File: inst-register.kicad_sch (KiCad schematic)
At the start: 20 parts

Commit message: Fix Clock
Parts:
- C13: value (none) -> 0.1µF; footprint (none) -> Capacitor_THT:C_Disc_D4.3mm_W1.9mm_P5.00mm
- D26, D27, D28, D29: value (none) -> BLUE; footprint (none) -> LED_THT:LED_D5.0mm
- D30, D31, D32, D33: value (none) -> YELLOW; footprint (none) -> LED_THT:LED_D5.0mm
- R40, R41, R42, R43, R44, R45, R46, R47: value (none) -> 220; footprint (none) -> Resistor_THT:R_Axial_DIN0207_L6.3mm_D2.5mm_P7.62mm_Horizontal
- U13: value (none) -> 74LS245; footprint (none) -> Package_DIP:DIP-20_W7.62mm
- U14, U15: value (none) -> 74LS173; footprint (none) -> Package_DIP:DIP-16_W7.62mm

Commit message: Fix
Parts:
- D26, D27, D28, D29, D30, D31, D32, D33: symbol Device:LED_ALT -> Device:LED
- U13: symbol 8bit-computer-rescue:74LS245 -> 74xx:74LS245
- U14, U15: symbol 8bit-computer-rescue:74LS173 -> 74xx:74LS173
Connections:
- net IR_4: now also D29.2 (A)
- net IR_5: now also D28.2 (A)
- net IR_6: now also D27.2 (A)
- net IR_7: now also D26.2 (A)
- net at R44.1: now also D30.1 (K)
- net at R40.1: now also D26.1 (K)
- net at R41.1: now also D27.1 (K)
- net at R42.1: now also D28.1 (K)
- net at R43.1: now also D29.1 (K)
- net at R45.1: now also D31.1 (K)
- net at R46.1: now also D32.1 (K)
- net at R47.1: now also D33.1 (K)
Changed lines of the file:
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@@
     (effects (font (size 1.524 1.524)) (justify left))
   )
-  (symbol (lib_id "Device:LED_ALT") (at 97.79 138.43 90) (unit 1)
+  (symbol (lib_id "Device:LED") (at 97.79 138.43 90) (unit 1)
     (in_bom yes) (on_board yes)
     (property "Reference" "D26" (id 0) (at 95.25 138.43 0))
@@
       (effects (font (size 1.27 1.27)) hide)
     )
-    (property "Datasheet" "" (id 3) (at 97.79 138.43 0)
-      (effects (font (size 1.27 1.27)) hide)
-    )
-  )
-  (symbol (lib_id "Device:LED_ALT") (at 120.65 138.43 90) (unit 1)
+    (property "Datasheet" "~" (id 3) (at 97.79 138.43 0)
+      (effects (font (size 1.27 1.27)) hide)
+    )
+    (pin "1")
+    (pin "2")
+  )
+  (symbol (lib_id "Device:LED") (at 120.65 138.43 90) (unit 1)
     (in_bom yes) (on_board yes)
     (property "Reference" "D29" (id 0) (at 118.11 138.43 0))
@@
       (effects (font (size 1.27 1.27)) hide)
     )
-    (property "Datasheet" "" (id 3) (at 120.65 138.43 0)
-      (effects (font (size 1.27 1.27)) hide)
-    )
-  )
-  (symbol (lib_id "Device:LED_ALT") (at 128.27 138.43 90) (unit 1)
+    (property "Datasheet" "~" (id 3) (at 120.65 138.43 0)
+      (effects (font (size 1.27 1.27)) hide)
+    )
+    (pin "1")
+    (pin "2")
+  )
+  (symbol (lib_id "Device:LED") (at 128.27 138.43 90) (unit 1)
     (in_bom yes) (on_board yes)
     (property "Reference" "D30" (id 0) (at 125.73 138.43 0))
@@
       (effects (font (size 1.27 1.27)) hide)
     )
-    (property "Datasheet" "" (id 3) (at 128.27 138.43 0)
-      (effects (font (size 1.27 1.27)) hide)
-    )
-  )
-  (symbol (lib_id "Device:LED_ALT") (at 135.89 138.43 90) (unit 1)
+    (property "Datasheet" "~" (id 3) (at 128.27 138.43 0)
+      (effects (font (size 1.27 1.27)) hide)
+    )
+    (pin "1")
+    (pin "2")
+  )
+  (symbol (lib_id "Device:LED") (at 135.89 138.43 90) (unit 1)
     (in_bom yes) (on_board yes)
     (property "Reference" "D31" (id 0) (at 133.35 138.43 0))
@@
       (effects (font (size 1.27 1.27)) hide)
     )
-    (property "Datasheet" "" (id 3) (at 135.89 138.43 0)
-      (effects (font (size 1.27 1.27)) hide)
-    )
+    (property "Datasheet" "~" (id 3) (at 135.89 138.43 0)
+      (effects (font (size 1.27 1.27)) hide)
+    )
+    (pin "1")
+    (pin "2")
   )
   (symbol (lib_id "Device:R") (at 128.27 149.86 0) (unit 1)
@@
     (pin "1")
   )
-  (symbol (lib_id "8bit-computer-rescue:74LS173") (at 132.08 64.77 270) (unit 1)
+  (symbol (lib_id "74xx:74LS173") (at 132.08 64.77 270) (unit 1)
     (in_bom yes) (on_board yes)
     (property "Reference" "U14" (id 0) (at 134.62 67.31 0))
@@
       (effects (font (size 1.27 1.27)) hide)
     )
-    (property "Datasheet" "" (id 3) (at 132.08 64.77 0)
-      (effects (font (size 1.27 1.27)) hide)
-    )
-  )
-  (symbol (lib_id "8bit-computer-rescue:74LS173") (at 172.72 64.77 270) (unit 1)
+    (property "Datasheet" "http://www.ti.com/lit/gpn/sn74LS173" (id 3) (at 132.08 64.77 0)
+      (effects (font (size 1.27 1.27)) hide)
+    )
+    (pin "1")
+    (pin "10")
+    (pin "11")
+    (pin "12")
+    (pin "13")
+    (pin "14")
+    (pin "15")
+    (pin "16")
+    (pin "2")
+    (pin "3")
+    (pin "4")
+    (pin "5")
+    (pin "6")
+    (pin "7")
+    (pin "8")
+    (pin "9")
+  )
+  (symbol (lib_id "74xx:74LS173") (at 172.72 64.77 270) (unit 1)
     (in_bom yes) (on_board yes)
     (property "Reference" "U15" (id 0) (at 175.26 67.31 0))
@@
       (effects (font (size 1.27 1.27)) hide)
     )
-    (property "Datasheet" "" (id 3) (at 172.72 64.77 0)
-      (effects (font (size 1.27 1.27)) hide)
-    )
-  )
-  (symbol (lib_id "8bit-computer-rescue:74LS245") (at 90.17 64.77 90) (unit 1)
+    (property "Datasheet" "http://www.ti.com/lit/gpn/sn74LS173" (id 3) (at 172.72 64.77 0)
+      (effects (font (size 1.27 1.27)) hide)
+    )
+    (pin "1")
+    (pin "10")
+    (pin "11")
+    (pin "12")
+    (pin "13")
+    (pin "14")
+    (pin "15")
+    (pin "16")
+    (pin "2")
+    (pin "3")
+    (pin "4")
+    (pin "5")
+    (pin "6")
+    (pin "7")
+    (pin "8")
+    (pin "9")
+  )
+  (symbol (lib_id "74xx:74LS245") (at 90.17 64.77 90) (unit 1)
     (in_bom yes) (on_board yes)
     (property "Reference" "U13" (id 0) (at 75.565 62.23 0)
@@
       (effects (font (size 1.27 1.27)) hide)
     )
-    (property "Datasheet" "" (id 3) (at 90.17 64.77 0)
-      (effects (font (size 1.27 1.27)) hide)
-    )
-  )
-  (symbol (lib_id "Device:LED_ALT") (at 105.41 138.43 90) (unit 1)
+    (property "Datasheet" "http://www.ti.com/lit/gpn/sn74LS245" (id 3) (at 90.17 64.77 0)
+      (effects (font (size 1.27 1.27)) hide)
+    )
+    (pin "1")
+    (pin "10")
+    (pin "11")
+    (pin "12")
+    (pin "13")
+    (pin "14")
+    (pin "15")
+    (pin "16")
+    (pin "17")
+    (pin "18")
+    (pin "19")
+    (pin "2")
+    (pin "20")
+    (pin "3")
+    (pin "4")
+    (pin "5")
+    (pin "6")
+    (pin "7")
+    (pin "8")
+    (pin "9")
+  )
+  (symbol (lib_id "Device:LED") (at 105.41 138.43 90) (unit 1)
     (in_bom yes) (on_board yes)
     (property "Reference" "D27" (id 0) (at 102.87 138.43 0))
@@
       (effects (font (size 1.27 1.27)) hide)
     )
-    (property "Datasheet" "" (id 3) (at 105.41 138.43 0)
-      (effects (font (size 1.27 1.27)) hide)
-    )
-  )
-  (symbol (lib_id "Device:LED_ALT") (at 113.03 138.43 90) (unit 1)
+    (property "Datasheet" "~" (id 3) (at 105.41 138.43 0)
+      (effects (font (size 1.27 1.27)) hide)
+    )
+    (pin "1")
+    (pin "2")
+  )
+  (symbol (lib_id "Device:LED") (at 113.03 138.43 90) (unit 1)
     (in_bom yes) (on_board yes)
     (property "Reference" "D28" (id 0) (at 110.49 138.43 0))
@@
       (effects (font (size 1.27 1.27)) hide)
     )
-    (property "Datasheet" "" (id 3) (at 113.03 138.43 0)
-      (effects (font (size 1.27 1.27)) hide)
-    )
-  )
-  (symbol (lib_id "Device:LED_ALT") (at 143.51 138.43 90) (unit 1)
+    (property "Datasheet" "~" (id 3) (at 113.03 138.43 0)
+      (effects (font (size 1.27 1.27)) hide)
+    )
+    (pin "1")
+    (pin "2")
+  )
+  (symbol (lib_id "Device:LED") (at 143.51 138.43 90) (unit 1)
     (in_bom yes) (on_board yes)
     (property "Reference" "D32" (id 0) (at 140.97 138.43 0))
@@
       (effects (font (size 1.27 1.27)) hide)
     )
-    (property "Datasheet" "" (id 3) (at 143.51 138.43 0)
-      (effects (font (size 1.27 1.27)) hide)
-    )
-  )
-  (symbol (lib_id "Device:LED_ALT") (at 151.13 138.43 90) (unit 1)
+    (property "Datasheet" "~" (id 3) (at 143.51 138.43 0)
+      (effects (font (size 1.27 1.27)) hide)
+    )
+    (pin "1")
+    (pin "2")
+  )
+  (symbol (lib_id "Device:LED") (at 151.13 138.43 90) (unit 1)
     (in_bom yes) (on_board yes)
     (property "Reference" "D33" (id 0) (at 148.59 138.43 0))
@@
       (effects (font (size 1.27 1.27)) hide)
     )
-    (property "Datasheet" "" (id 3) (at 151.13 138.43 0)
-      (effects (font (size 1.27 1.27)) hide)
-    )
+    (property "Datasheet" "~" (id 3) (at 151.13 138.43 0)
+      (effects (font (size 1.27 1.27)) hide)
+    )
+    (pin "1")
+    (pin "2")
   )
   (symbol (lib_id "Device:R") (at 97.79 149.86 0) (unit 1)

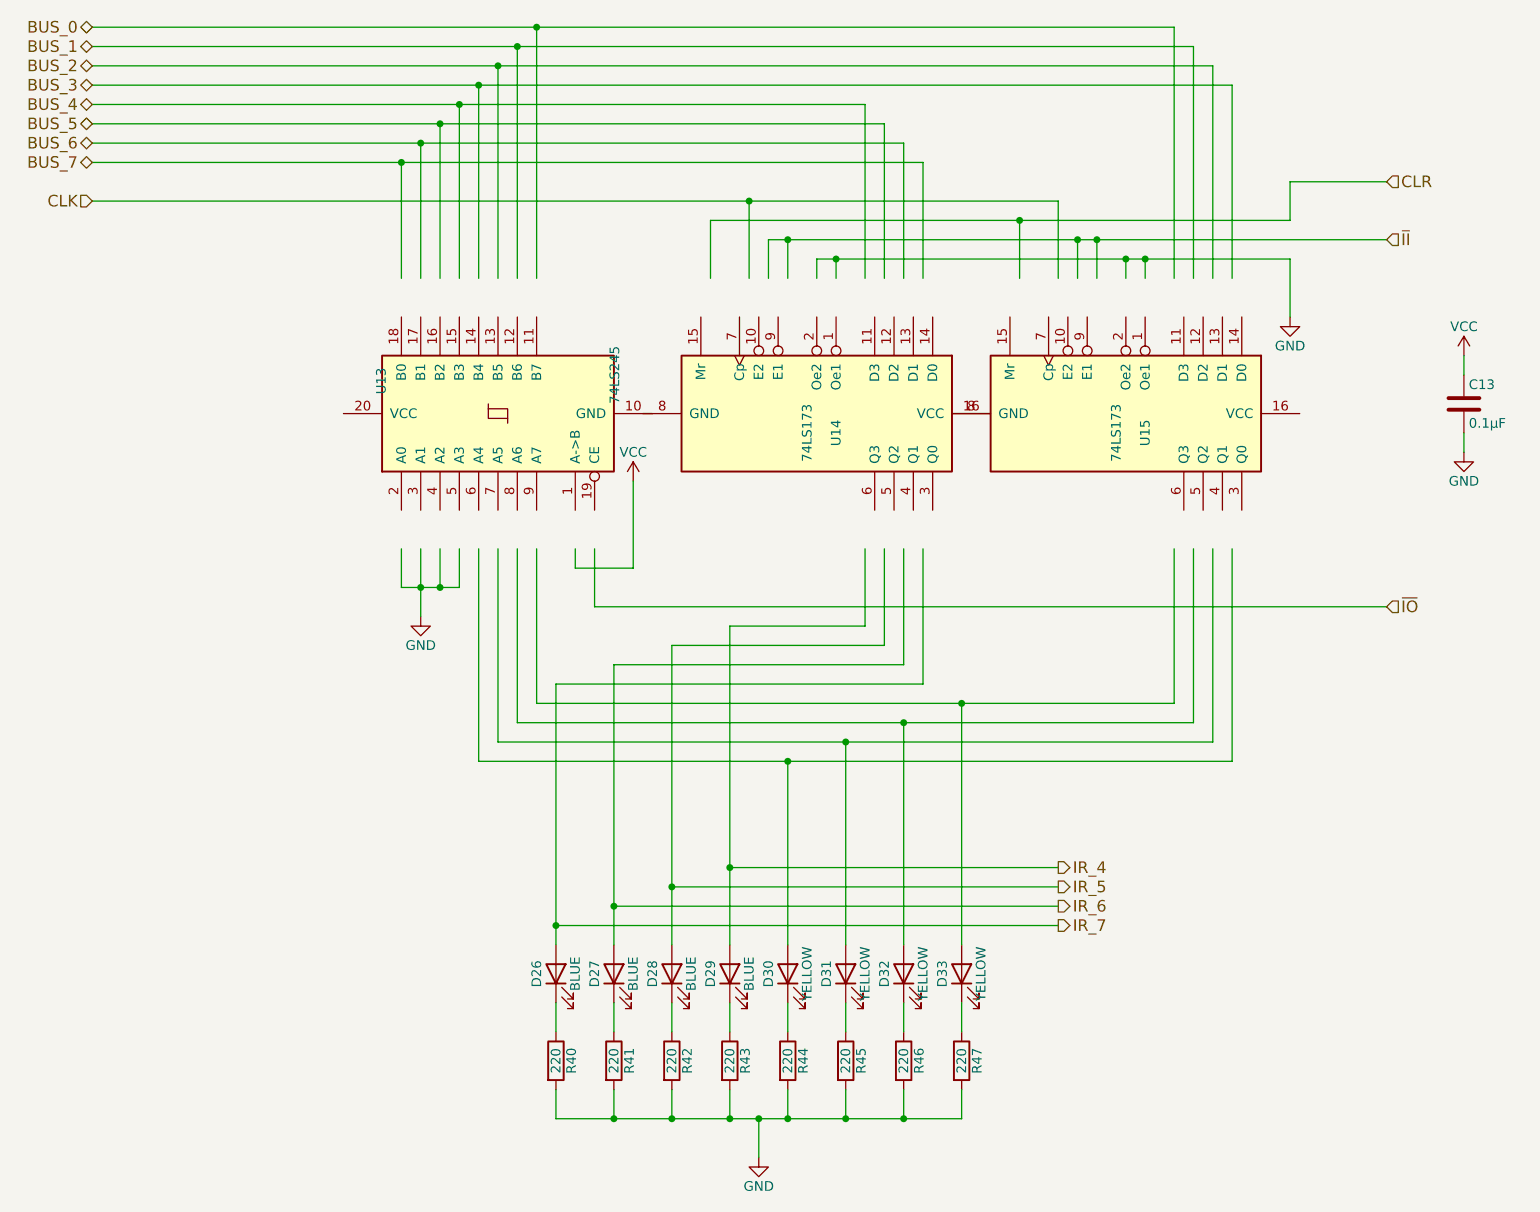
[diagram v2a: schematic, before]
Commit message: Fix instruction register
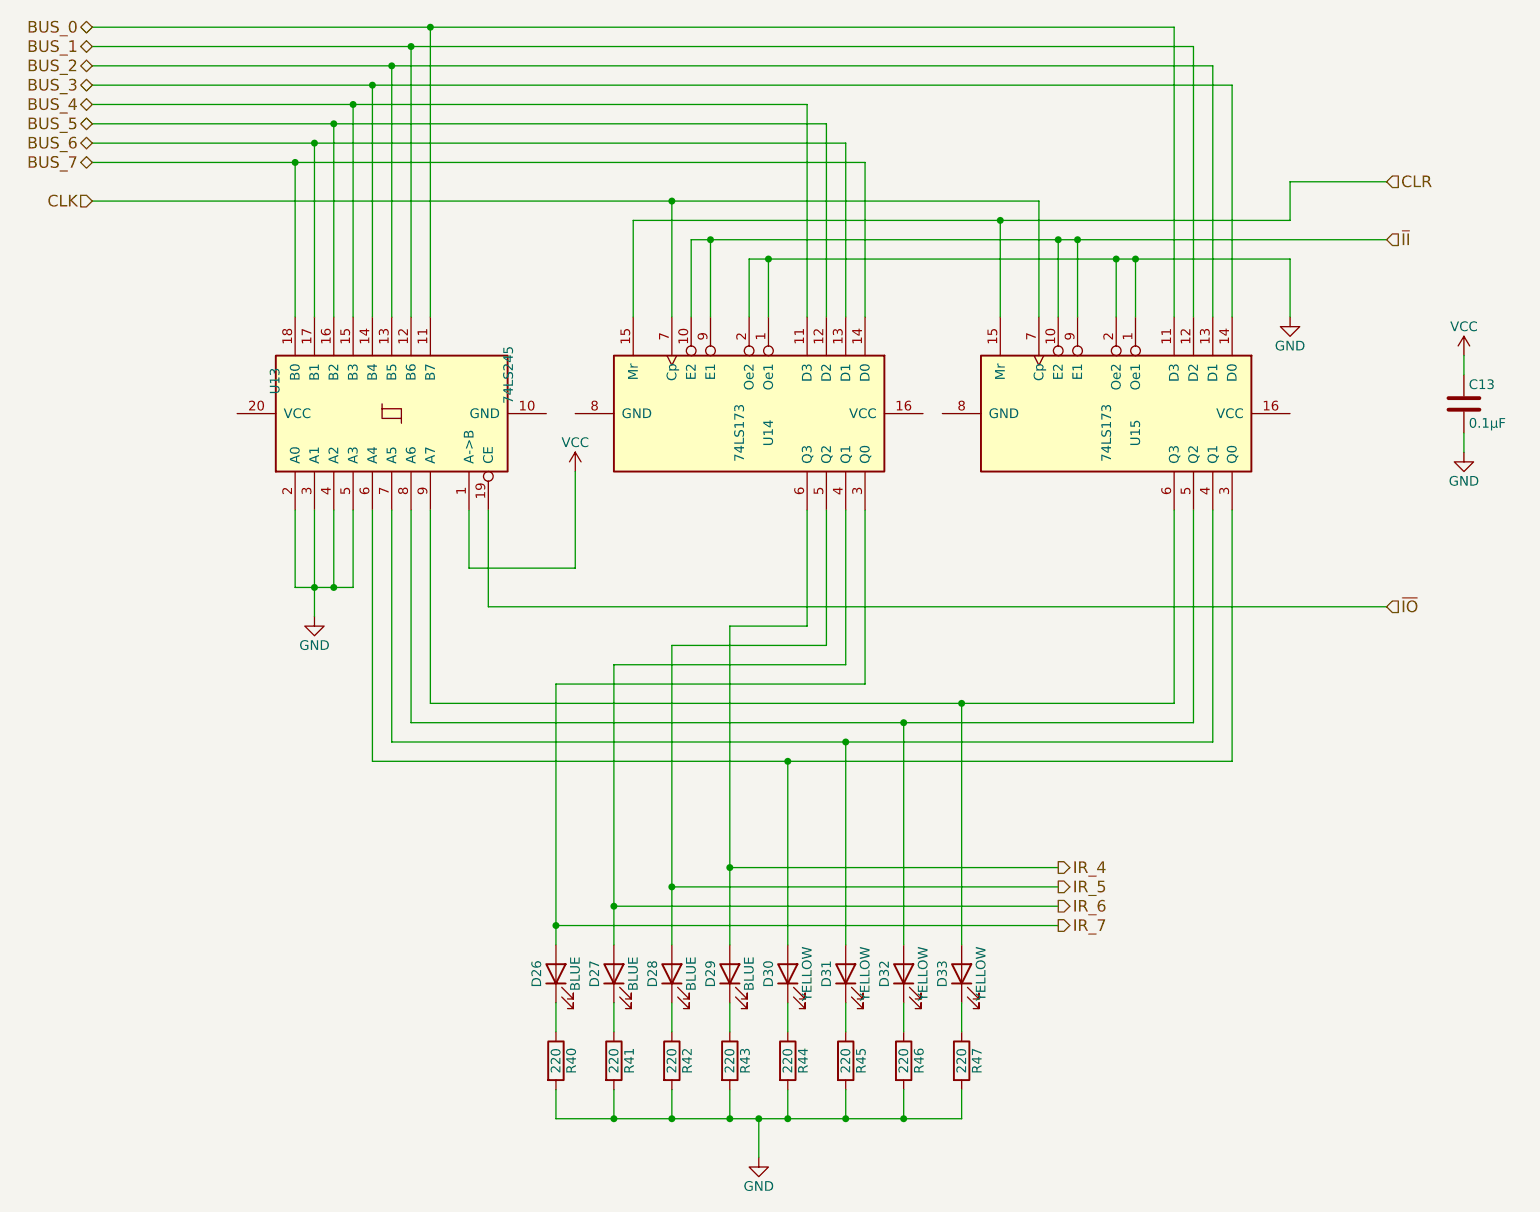
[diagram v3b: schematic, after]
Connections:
- net BUS_0: now also U13.11 (B7), U15.11 (D3)
- net BUS_1: now also U13.12 (B6), U15.12 (D2)
- net BUS_2: now also U13.13 (B5), U15.13 (D1)
- net BUS_3: now also U13.14 (B4), U15.14 (D0)
- net BUS_4: now also U13.15 (B3), U14.11 (D3)
- net BUS_5: now also U13.16 (B2), U14.12 (D2)
- net BUS_6: now also U13.17 (B1), U14.13 (D1)
- net BUS_7: now also U13.18 (B0), U14.14 (D0)
- net CLK: now also U14.7 (Cp), U15.7 (Cp)
- net CLR: now also U14.15 (Mr), U15.15 (Mr)
- net GND: now also U13.2 (A0), U13.3 (A1), U13.4 (A2), U13.5 (A3), U14.1 (Oe1), U14.2 (Oe2), U15.1 (Oe1), U15.2 (Oe2)
- net IR_4: now also U14.6 (Q3)
- net IR_5: now also U14.5 (Q2)
- net IR_6: now also U14.4 (Q1)
- net IR_7: now also U14.3 (Q0)
- net VCC: now also U13.1 (A->B)
- net ~{II}: now also U14.10 (E2), U14.9 (E1), U15.10 (E2), U15.9 (E1)
- net ~{IO}: now also U13.19 (CE)
- net at D30.2 (A): now also U13.6 (A4), U15.3 (Q0)
- net at D31.2 (A): now also U13.7 (A5), U15.4 (Q1)
- net at U15.5 (Q2): now also D32.2 (A), U13.8 (A6)
- net at U15.6 (Q3): now also D33.2 (A), U13.9 (A7)
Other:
- moved on the sheet: U13, U14, U15
